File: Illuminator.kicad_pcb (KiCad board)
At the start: 2 copper layers, 17 parts, among them J0 Conn_01x03_Male, Q0 DMG1012UW

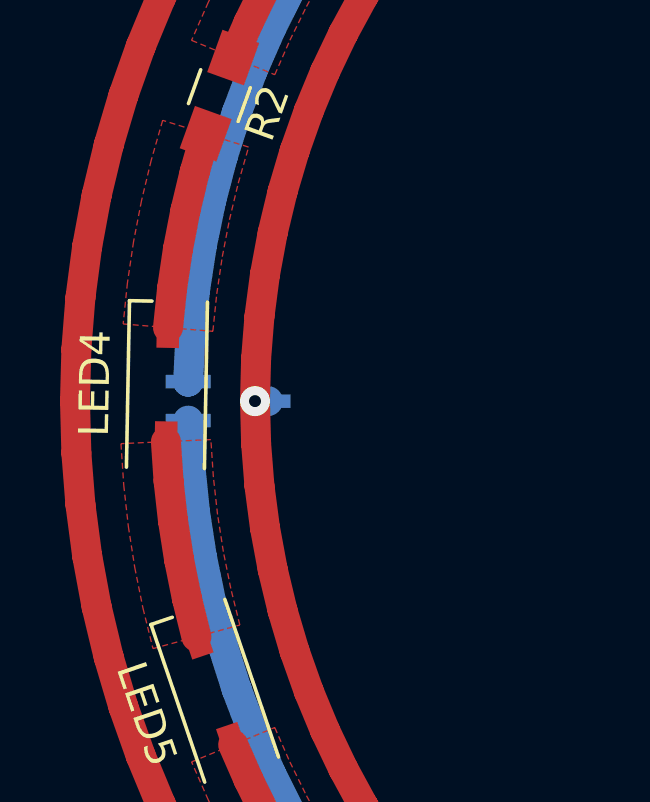
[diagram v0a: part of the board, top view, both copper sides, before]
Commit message: Adding copper pours around the mosfet
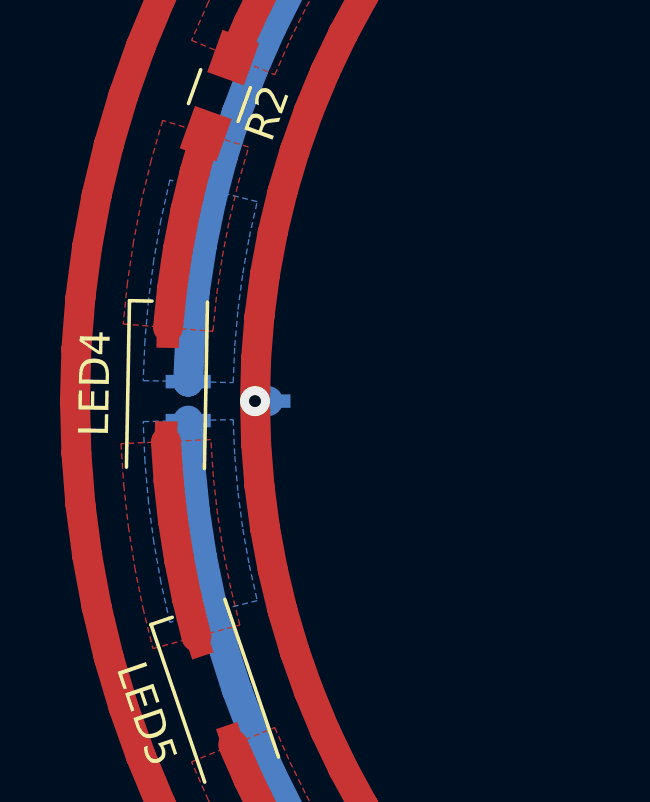
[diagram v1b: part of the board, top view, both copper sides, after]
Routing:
- added copper zone on B.Cu, net /TO_3V3
- added copper zone on B.Cu, net /TO_GND
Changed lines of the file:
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@@
+    )
+  )
+  (zone (net 3) (net_name /TO_3V3) (layer B.Cu) (hatch edge 0.508)
+    (connect_pads yes (clearance 0.508))
+    (min_thickness 0.254)
+    (fill yes (arc_segments 16) (thermal_gap 0.508) (thermal_bridge_width 0.508) (smoothing fillet) (radius 0.5))
+    (polygon
+      (pts
+        (xy 72.271871 100.616649) (xy 72.32581 101.835376) (xy 72.43329 103.050553) (xy 72.594102 104.259827) (xy 72.807935 105.460861)
+        (xy 73.074377 106.651329) (xy 70.161922 107.370781) (xy 69.866661 106.051544) (xy 69.629698 104.720599) (xy 69.451492 103.380521)
+        (xy 69.332386 102.033903) (xy 69.272613 100.68335)
+      )
     )
   )
@@
       )
     )
+  )
+  (zone (net 2) (net_name /TO_GND) (layer B.Cu) (hatch edge 0.508)
+    (connect_pads yes (clearance 0.508))
+    (min_thickness 0.254)
+    (fill yes (arc_segments 16) (thermal_gap 0.508) (thermal_bridge_width 0.508) (smoothing fillet) (radius 0.5))
+    (polygon
+      (pts
+        (xy 72.271871 99.38335) (xy 72.32581 98.164623) (xy 72.43329 96.949446) (xy 72.594102 95.740172) (xy 72.807935 94.539138)
+        (xy 73.074377 93.34867) (xy 70.161922 92.629218) (xy 69.866661 93.948455) (xy 69.629698 95.2794) (xy 69.451492 96.619478)
+        (xy 69.332386 97.966096) (xy 69.272613 99.316649)
+      )
+    )

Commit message: Added some text
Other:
- board outline added: 70 x 70 mm
- board text added: "3V3"
- board text added: "5V"
- board text added: "GND"
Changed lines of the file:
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@@
 (general
   (thickness 1.6)
-  (drawings 0)
+  (drawings 5)
   (tracks 955)
   (zones 0)
@@
     (tags "Surface mounted pin header SMD 1x03 1.27mm single row style1 pin1 left")
     (attr smd)
-    (fp_text reference J0 (at 0 2.965) (layer B.SilkS)
+    (fp_text reference J0 (at -2.707386 0 -90) (layer B.SilkS)
       (effects (font (size 1 1) (thickness 0.15)) (justify mirror))
     )
-    (fp_text value Conn_01x03_Male (at 0 -2.965) (layer B.Fab)
+    (fp_text value Conn_01x03_Male (at -4.707386 0 -90) (layer B.Fab) hide
       (effects (font (size 1 1) (thickness 0.15)) (justify mirror))
     )
@@
     (tags "SOT-323 SC-70 Handsoldering")
     (attr smd)
-    (fp_text reference Q0 (at 0 2) (layer B.SilkS)
+    (fp_text reference Q0 (at -3.102242 0 90) (layer B.SilkS)
       (effects (font (size 1 1) (thickness 0.15)) (justify mirror))
     )
-    (fp_text value DMG1012UW (at 0 -2.05) (layer B.Fab)
+    (fp_text value DMG1012UW (at -5.102242 0 90) (layer B.Fab)
       (effects (font (size 1 1) (thickness 0.15)) (justify mirror))
     )
@@
     )
   )
+  (gr_text 3V3 (at 126.652679 104.316793 260.8) (layer B.SilkS)
+    (effects (font (size 1.5 1.5) (thickness 0.3)) (justify mirror))
+  )
+  (gr_text GND (at 126.652679 95.683208 279.2) (layer B.SilkS)
+    (effects (font (size 1.5 1.5) (thickness 0.3)) (justify mirror))
+  )
+  (gr_text 5V (at 132.93956 98.003664 273.5) (layer B.SilkS)
+    (effects (font (size 1.5 1.5) (thickness 0.3)) (justify mirror))
+  )
+  (gr_circle (center 100 100) (end 135 100) (layer Edge.Cuts) (width 0.1))
+  (gr_circle (center 100 100) (end 125 100) (layer Edge.Cuts) (width 0.1))
   (via (at 133 100) (size 1) (drill 0.4) (layers F.Cu B.Cu) (net 1))
   (segment (start 132.207386 100) (end 133 100) (width 1) (layer B.Cu) (net 1))

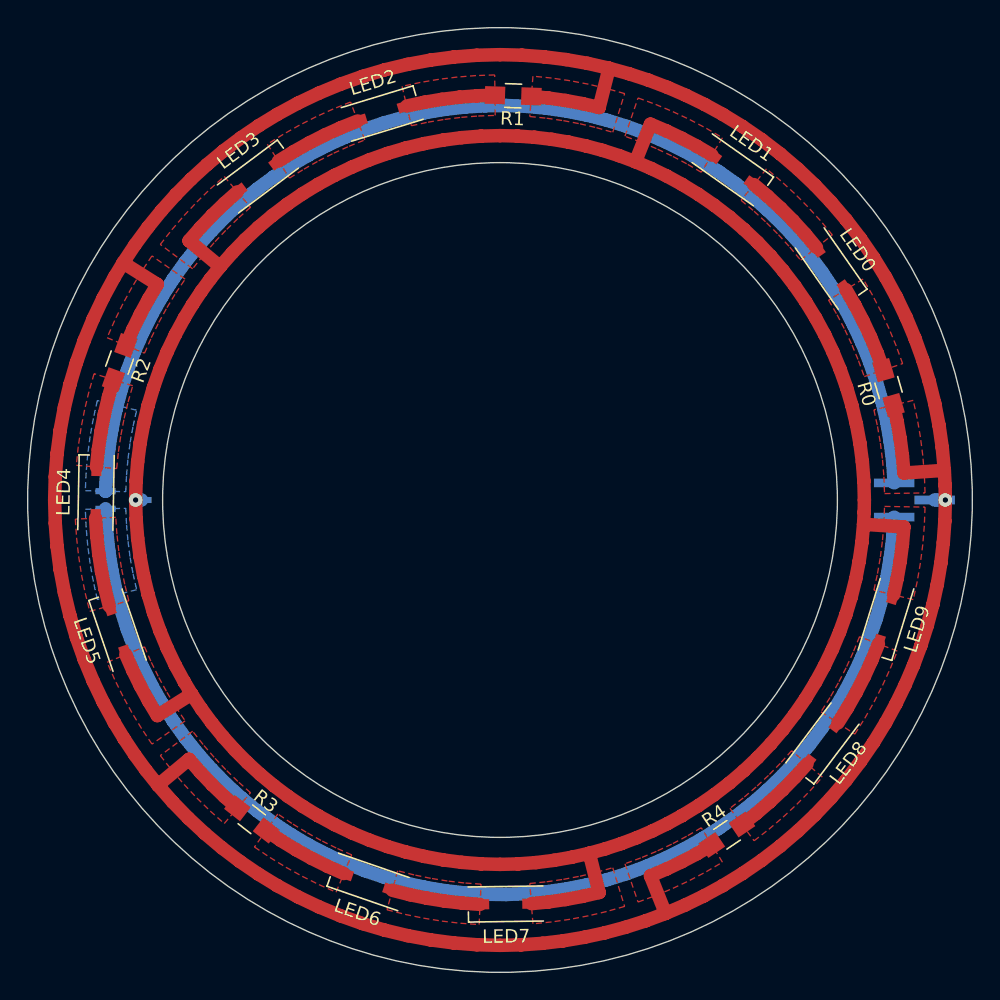
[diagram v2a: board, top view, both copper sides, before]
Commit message: Using tighter radius.
Added drawings and cuts for picamera
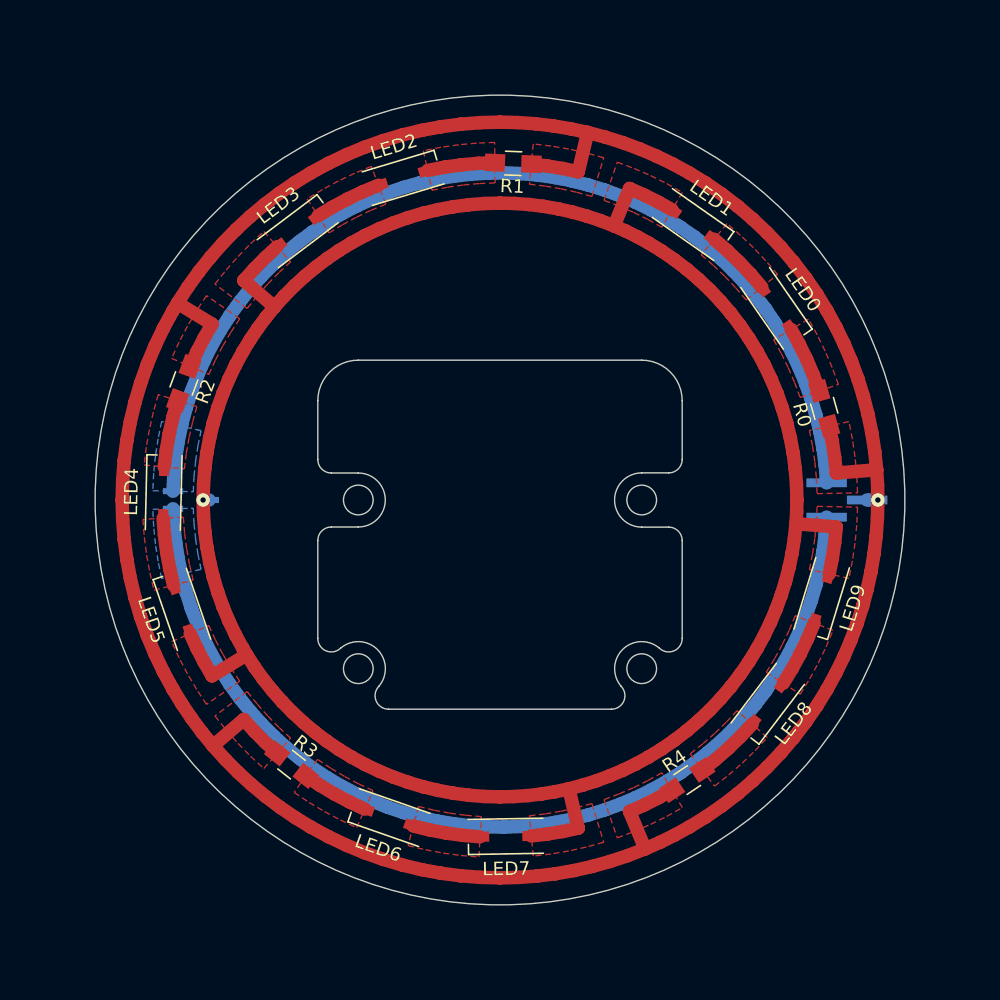
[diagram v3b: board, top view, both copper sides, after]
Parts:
- moved LED6 5.01 mm to (91.8, 123.5), turned to 160.737 degrees
- moved LED8 5.01 mm to (119.8, 115.1), turned to 232.737 degrees
- moved LED0 5.01 mm to (120.5, 85.8), turned to 304.737 degrees
- moved LED2 5.01 mm to (92.8, 76.1), turned to 16.7368 degrees
- moved LED4 5.01 mm to (75.1, 99.5), turned to 88.7368 degrees
- moved LED3 5.01 mm to (85.0, 80.1), turned to 36.9747 degrees
- moved LED1 5.01 mm to (114.3, 79.6), turned to 324.975 degrees
- moved LED9 5.01 mm to (123.8, 107.3), turned to 252.975 degrees
- moved LED7 5.01 mm to (100.4, 124.9), turned to 180.975 degrees
- moved LED5 5.01 mm to (76.4, 108.1), turned to 108.975 degrees
- moved R3 5.01 mm to (84.5, 119.6), turned to 321.762 degrees
- moved R4 5.01 mm to (113.9, 120.8), turned to 33.7621 degrees
- moved R0 5.01 mm to (124.0, 93.2), turned to 105.762 degrees
- moved R2 5.01 mm to (76.6, 91.4), turned to 249.762 degrees
- moved R1 5.01 mm to (101.0, 75.1), turned to 177.762 degrees
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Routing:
- net Net-(LED1-Pad1): track 210.5 -> 171.3 mm
- net /TO_5V: track 248.6 -> 209.3 mm
- net /TO_GND: track 89.9 -> 74.2 mm
- net /TO_3V3: track 89.9 -> 74.2 mm
- net Net-(LED2-Pad1): track 6.60 -> 5.03 mm
- net Net-(LED0-Pad1): track 6.60 -> 5.03 mm
- net Net-(LED2-Pad2): track 6.60 -> 5.03 mm
- net Net-(LED4-Pad2): track 6.60 -> 5.03 mm
- net Net-(LED6-Pad2): track 6.60 -> 5.03 mm
- net Net-(LED6-Pad1): track 6.60 -> 5.03 mm
- net Net-(LED0-Pad2): track 6.60 -> 5.03 mm
- net Net-(LED8-Pad1): track 6.60 -> 5.03 mm
- net Net-(LED8-Pad2): track 6.60 -> 5.03 mm
- net Net-(LED4-Pad1): track 6.60 -> 5.03 mm
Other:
- board size 70 x 70 mm -> 60 x 60 mm
- board text removed: "3V3"
- board text removed: "5V"
- board text removed: "GND"

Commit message: Added GND 3V3 5V text
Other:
- board text added: "3V3"
- board text added: "5V"
- board text added: "GND"
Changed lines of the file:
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@@
 (general
   (thickness 1.6)
-  (drawings 73)
+  (drawings 76)
   (tracks 935)
   (zones 0)
@@
 (page A4)
 (layers
-  (0 F.Cu signal)
+  (0 F.Cu signal hide)
   (31 B.Cu signal)
   (32 B.Adhes user)
@@
     (fp_line (start -3.025 -1.55) (end -3.025 1.55) (layer F.CrtYd) (width 0.05))
     (fp_circle (center 0 0) (end 0.9 0) (layer F.Fab) (width 0.1))
-    (pad 2 smd rect (at 1.9 0 36.97474287) (size 1.35 0.75) (layers F.Cu F.Paste F.Mask)
+    (pad 2 smd rect (at 1.9 -0.000001 36.97474287) (size 1.35 0.75) (layers F.Cu F.Paste F.Mask)
       (net 7 "Net-(LED2-Pad1)"))
-    (pad 1 smd rect (at -1.9 0 36.97474287) (size 1.35 0.75) (layers F.Cu F.Paste F.Mask)
+    (pad 1 smd rect (at -1.9 0.000001 36.97474287) (size 1.35 0.75) (layers F.Cu F.Paste F.Mask)
       (net 6 "Net-(LED1-Pad1)"))
     (model /Users/Spak/Desktop/RatcamIlluminator/Ratcam.pretty/LED-GW_2.3x2.3mm.wrl
@@
       (effects (font (size 0.5 0.5) (thickness 0.075)))
     )
-    (pad 2 smd rect (at 1.35 0 249.7620528) (size 1.5 1.3) (layers F.Cu F.Paste F.Mask)
+    (pad 2 smd rect (at 1.350001 0 249.7620528) (size 1.5 1.3) (layers F.Cu F.Paste F.Mask)
       (net 10 "Net-(LED4-Pad2)"))
-    (pad 1 smd rect (at -1.35 0 249.7620528) (size 1.5 1.3) (layers F.Cu F.Paste F.Mask)
+    (pad 1 smd rect (at -1.350001 0 249.7620528) (size 1.5 1.3) (layers F.Cu F.Paste F.Mask)
       (net 1 /TO_5V))
     (model ${KISYS3DMOD}/Resistors_SMD.3dshapes/R_0805.wrl
@@
     )
   )
+  (gr_text 3V3 (at 121.519247 104.574057 258) (layer B.SilkS)
+    (effects (font (size 1.5 1.5) (thickness 0.3)) (justify mirror))
+  )
+  (gr_text GND (at 121.519247 95.425943 282) (layer B.SilkS)
+    (effects (font (size 1.5 1.5) (thickness 0.3)) (justify mirror))
+  )
+  (gr_text 5V (at 127.928844 98.005083 274.1) (layer B.SilkS)
+    (effects (font (size 1.5 1.5) (thickness 0.3)) (justify mirror))
+  )
   (gr_line (start 109.5 100) (end 111.5 100) (layer Dwgs.User) (width 0.1))

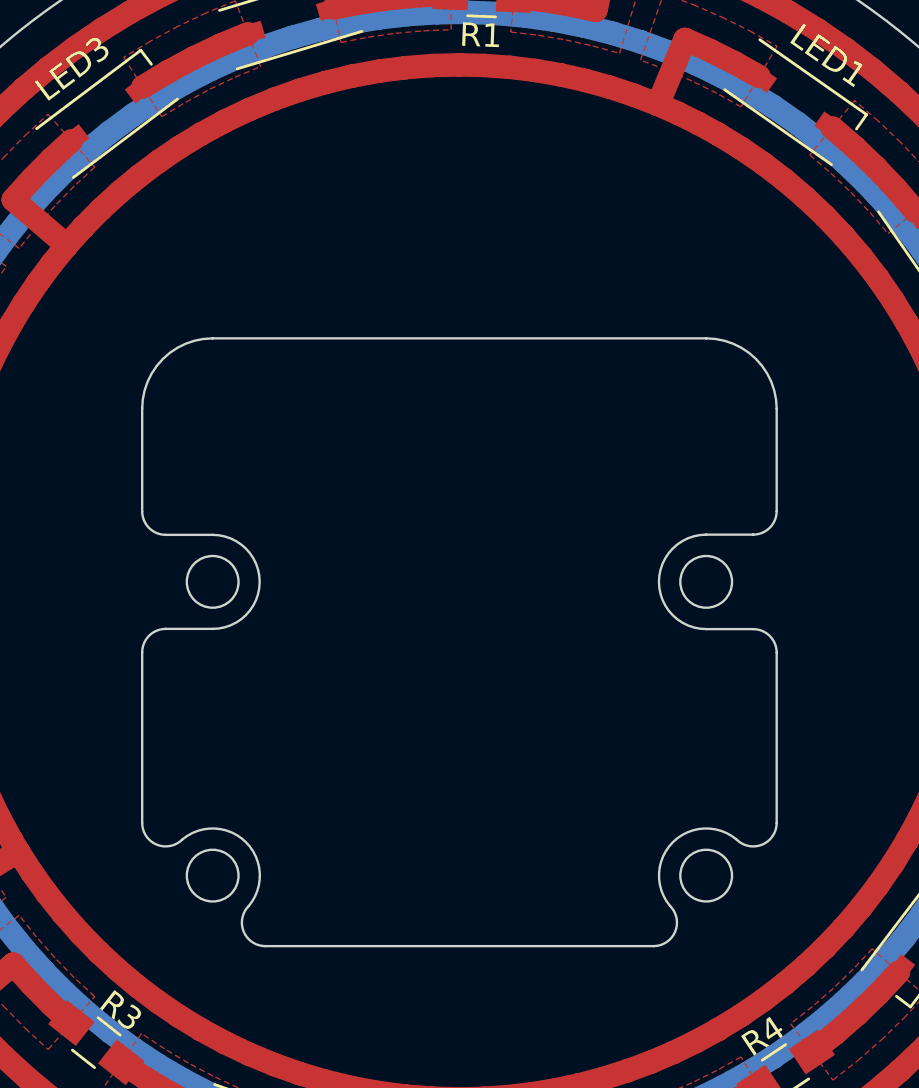
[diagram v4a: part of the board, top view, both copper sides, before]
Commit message: Added correct edge cuts and outline DXF, plus QR code
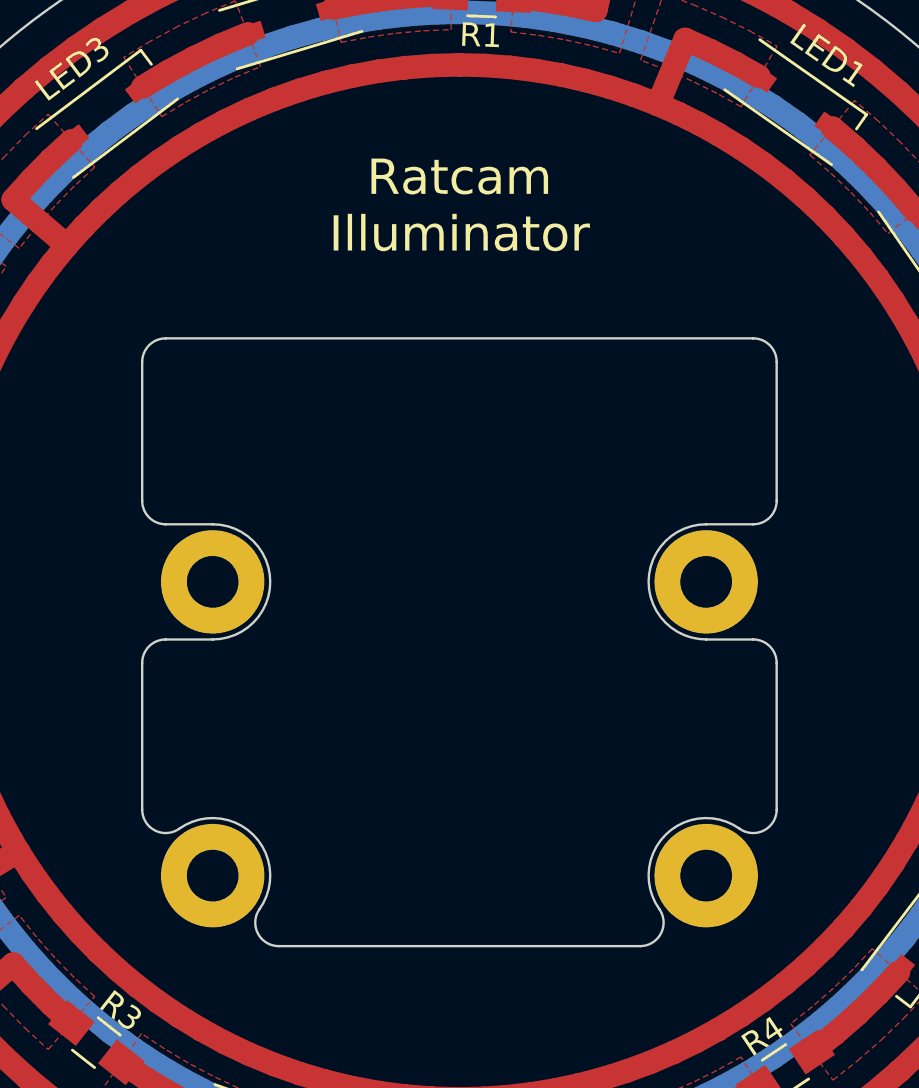
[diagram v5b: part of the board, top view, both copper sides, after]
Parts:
- added QRCode: http://bit.ly/2m9yLHR, Ratcam:QRCode, B.Cu at (100.0, 83.0)
- added REF**: MountingHole_2.2mm_M2_Pad, Mounting_Holes:MountingHole_2.2mm_M2_Pad, F.Cu at (110.5, 112.5)
- added REF**: MountingHole_2.2mm_M2_Pad, Mounting_Holes:MountingHole_2.2mm_M2_Pad, F.Cu at (89.5, 112.5)
- added REF**: MountingHole_2.2mm_M2_Pad, Mounting_Holes:MountingHole_2.2mm_M2_Pad, F.Cu at (89.5, 100.0)
- added REF**: MountingHole_2.2mm_M2_Pad, Mounting_Holes:MountingHole_2.2mm_M2_Pad, F.Cu at (110.5, 100.0)
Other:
- outline, holes or cut-outs redrawn
- board text added: "Ratcam Illuminator"
